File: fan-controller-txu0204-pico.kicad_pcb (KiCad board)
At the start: 2 copper layers, 21 x 67.7 mm, 58 parts, among them CN1 PWR, CN2 RaspberryPi_Pico, CN3 RaspberryPi_Pico, Q1 RU1C002ZP, U1 TPS259472A, U2 TXU0204, U3 TXU0204

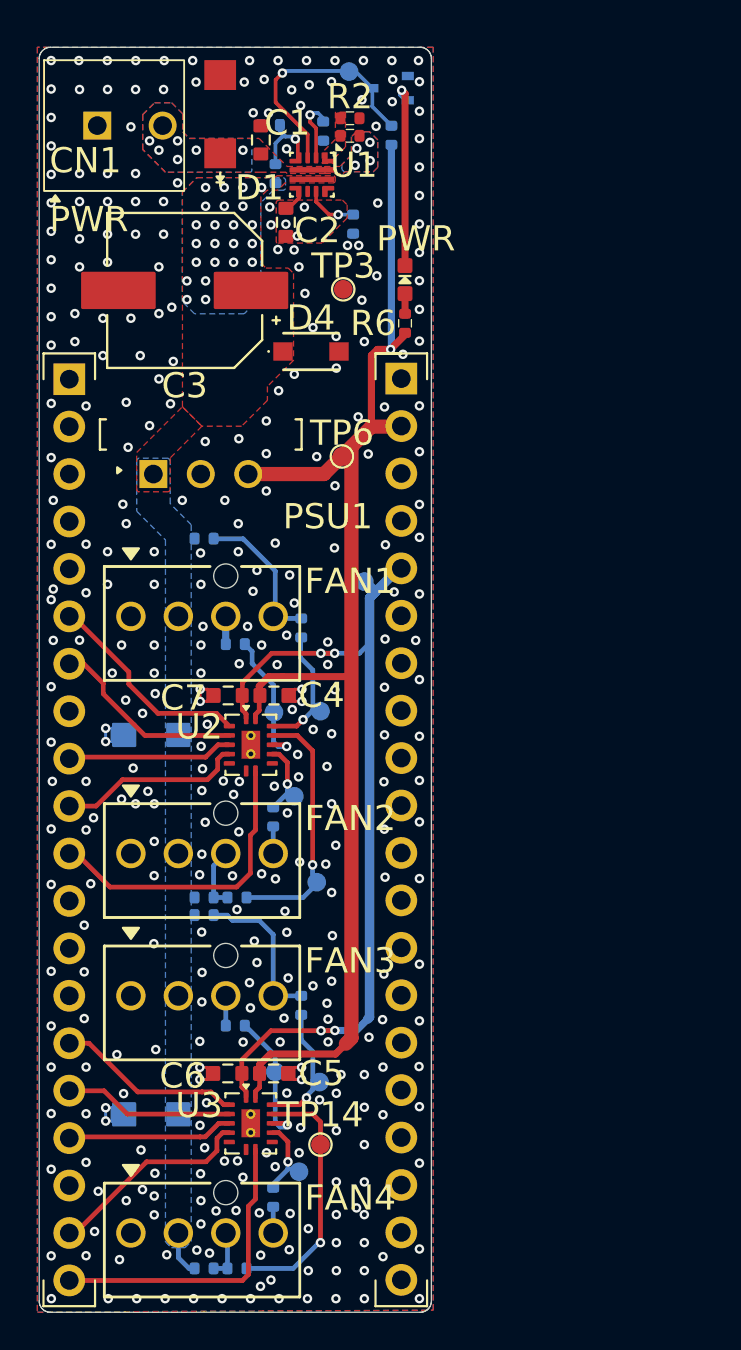
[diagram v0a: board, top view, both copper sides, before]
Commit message: tl;dr: switched to 4-layer pcb, overhauled 12vdc rail and protections, added 5vdc ORing ======================================================================== added:   ./       .gitignore - ignore lockfile
------------------------------------------------------------------------
removed:
  licenses/ - switched fonts to all WebPlus_ToshibaSat_8x14 and 9x16
      curie-LICENSE.txt
      curie-NOTICE.txt
      scientifica-LICENSE.txt
      scientifica-NOTICE.txt

------------------------------------------------------------------------
modified:
  ./
      README.md - updated to reflect changes in design
      fan-controller-pico_hmi.kicad_sch - added connector circuit, added
        pico pin connections
      fan-controller-txu0204-pico.kicad_pcb - changed to 4-layer design,
        changed protection circuit designs to use p-fet and polyfuse,
        split 12vdc rail into separate lines for fans and dc-dc
        converter, added lm66200 ORing diode, changed various netclass
        clearances, adjusted positions of tvs diodes for the fans'
        +12vdc pins
      fan-controller-txu0204-pico.kicad_sch - removed efuse, switched to
        p-fet reverse polarity protection, polyfuse for dc-dc converter,
        changed tvs diode for power connector to something more robust,
        added lm66200 ORing dual ideal diode for dc-dc converter 5v
        output and vbus to vsys control
      fan-controller-txu0204-pico.kicad_pro - see above
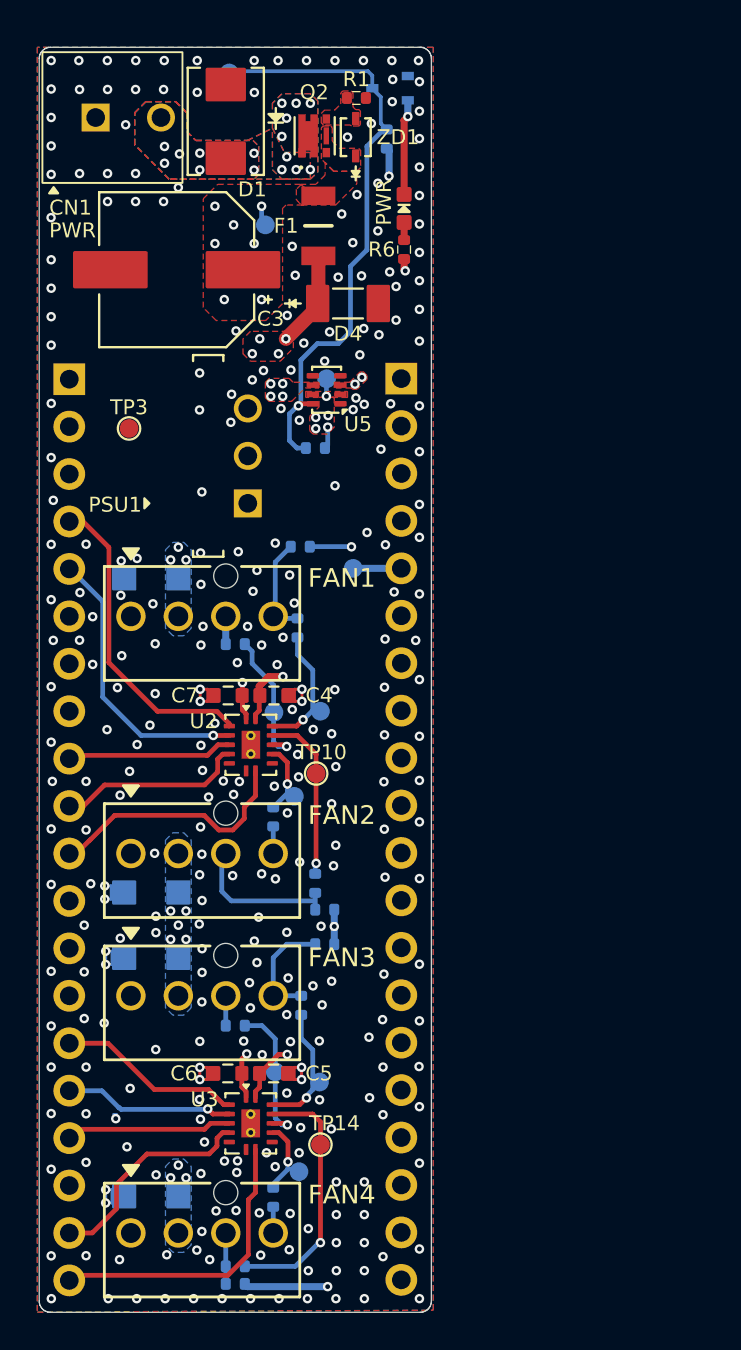
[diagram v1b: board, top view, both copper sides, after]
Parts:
- removed C1: 10uF, lsc-capacitors-added:C_GRM18_0603_1608Metric_MURATA
- removed C2: 0.56nF, lsc-capacitors-added:C_GRM18_0603_1608Metric_MURATA
- removed R2: 97.6k, lsc-resistor:R_RK37H_0402_1005Metric_KOA
- removed R3: 390k, lsc-resistor:R_RK37H_0402_1005Metric_KOA
- removed R4: 2.43k, lsc-resistor:R_RK37H_0402_1005Metric_KOA
- removed R5: 47k, lsc-resistor:R_RK37H_0402_1005Metric_KOA
- removed R7: 5.5k, lsc-resistor:R_RK37H_0402_1005Metric_KOA
- removed U1: TPS259472A, lsc-qfn:VFQFN10_RPW0010A_TI
- added D5: SMF12A, lsc-diode-smd:D_SOD-123F_EATON, B.Cu at (66.1, 92.2)
- added D6: SMF12A, lsc-diode-smd:D_SOD-123F_EATON, B.Cu at (66.1, 88.8)
- added F1: 2016L150/33DR, lsc-polyfuse:PTS1206_FUSC3216X68N_EATON, F.Cu at (75.0, 53.0)
- added Q2: DMP3014SFDE, lsc-dfn-vdfn-tdfn:TRANS_6-UDFN_U-DFN2020-6-E_DIO, F.Cu at (74.8, 48.2)
- added R9: 5.62k, lsc-resistor:R_RK37H_0402_1005Metric_KOA, B.Cu at (74.9, 65.0)
- added U5: LM66200, lsc-standard-chip-carrier:SOT-583_SOT-5X3_DRL0008A_TEX, F.Cu at (75.5, 61.8)
- added ZD1: MM3Z20B-AQ, lsc-diode-smd:D_SOD-323F_SOD323F_DIODES, F.Cu at (77.0, 48.3)
- CN2, CN3, TP6: moved to B.Cu
- D1: value TPSMA6L12A -> SMAJ16CA; footprint lsc-diode-smd:DIO_DO221AC_TPSMA6LSeries_LTF -> lsc-diode-smd:DIO_SMB_LOWVOLTAGE_DIODES
- D4: value RBS1MM40A -> SGL1-20; footprint lsc-diode-smd:CR_RBS1MM_ROM -> lsc-diode-smd:DIO_DO213AA_MINIMELF
- R1: value 470k -> 274
- R11, R12, R15, R16, R17, R18, R23, R24: value 10k -> 750
- R21, R22, R25, R26: value 7.5k -> 750
- TP10: moved to F.Cu
- moved TP3 13.7 mm to (64.9, 63.9)
- moved D2 8.38 mm to (66.1, 71.9)
- moved R22 6.65 mm to (75.4, 91.5), turned to 0 degrees
- moved R25 6.49 mm to (75.4, 89.7), turned to 0 degrees
- moved TP8 6.42 mm to (70.3, 44.9)
- moved TP10 5.82 mm to (74.9, 82.4)
- moved R21 5.17 mm to (74.1, 70.2), turned to 0 degrees
- moved D3 4.39 mm to (66.1, 105.0)
- moved R23 4.26 mm to (74.9, 88.3), turned to 90 degrees
- moved TP6 4.24 mm to (75.5, 61.2)
- moved R6 3.95 mm to (79.6, 54.3)
- moved LD1 3.81 mm to (79.6, 52.1)
- moved TP2 3.67 mm to (72.2, 53.0)
- moved D4 3.24 mm to (76.6, 57.2)
- moved PSU1 2.44 mm to (71.1, 65.4), turned to 90 degrees
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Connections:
- net /3V3 renamed +3.3VDC
- net /PWRGD renamed /LM66200_STAT
- C3 pad 1: /+12V_PROTECTED -> +12VDC
- C4 pad 1: /VSYS -> +5VDC
- C5 pad 1: /VSYS -> +5VDC
- CN2 pad 4: /GPIO2 -> /PICO_PWM_FAN1
- CN2 pad 5: /GPIO3 -> /PICO_PWM_FAN2
- CN2 pad 6: /PICO_PWM_FAN1 -> /Fan Controller Pico: HMI/I2C_SDA
- CN2 pad 7: /PICO_PWM_FAN2 -> /Fan Controller Pico: HMI/I2C_SCL
- CN3 pad 39: /VSYS -> +5VDC
- CN3 pad 40: /VBUS -> VBUS
- D2 pad 1: /+12V_PROTECTED -> +12VDC
- D3 pad 1: /+12V_PROTECTED -> +12VDC
- D4 pad 1: /+12V_PROTECTED -> /+12V_FUSED_PSU1
- FAN1 pad 2: /+12V_PROTECTED -> +12VDC
- FAN2 pad 2: /+12V_PROTECTED -> +12VDC
- FAN3 pad 2: /+12V_PROTECTED -> +12VDC
- FAN4 pad 2: /+12V_PROTECTED -> +12VDC
- PSU1 pad 1: /+12V_PROTECTED -> /+12V_FUSED_PSU1
- PSU1 pad 3: /VSYS -> /5V_PSU1_OUT
- R1 pad 1: /EN/UVLO -> GND
- R1 pad 2: /+12V_UNPROTECTED -> /V_{GS}_LIM
- R21 pad 2: /+12V_PROTECTED -> +5VDC
- R22 pad 2: /+12V_PROTECTED -> +5VDC
- R25 pad 2: /+12V_PROTECTED -> +5VDC
- R26 pad 2: /+12V_PROTECTED -> +5VDC
- R6 pad 2: /VSYS -> +5VDC
- R8 pad 2: /VSYS -> +5VDC
- TP2 pad 1: /+12V_PROTECTED -> +12VDC
- TP6 pad 1: /VSYS -> +5VDC
- U2 pad 14: /VSYS -> +5VDC
- U3 pad 14: /VSYS -> +5VDC
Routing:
- net +5VDC: track 0.00 -> 89.8 mm, vias 0 -> 12
- net /VSYS: track 72.5 -> 0.00 mm, vias 1 -> 0
- net /LM66200_STAT: track 13.1 -> 32.0 mm
- net /+12V_FUSED_PSU1: track 0.00 -> 15.5 mm, vias 0 -> 4
- net /PICO_PWM_FAN1: track 11.2 -> 16.8 mm
- net Net-(LD1-K): track 10.1 -> 5.29 mm
- net Net-(FAN2-Pin_3): track 3.37 -> 8.19 mm
- net /PICO_PWM_FAN2: track 10.5 -> 15.3 mm, vias 0 -> 1
- net /PWM_FAN2: track 13.6 -> 9.18 mm
- net /PGTH: track 4.35 -> 0.00 mm, vias 1 -> 0
- net /OVCSEL: track 3.48 -> 0.00 mm, vias 1 -> 0
- net /ILIM: track 2.82 -> 0.00 mm, vias 1 -> 0
- net /ENABLE_FAN1FAN2: track 16.3 -> 13.6 mm
- net Net-(FAN1-Pin_4): track 8.10 -> 5.53 mm
- net /+12V_PROTECTED: track 2.43 -> 0.00 mm, vias 23 -> 0
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- added copper zone on B.Cu, net +12VDC
- added copper zone on F.Cu, net +12VDC
- added copper zone on In2.Cu, net +12VDC
- added copper zone on F.Cu, net +5VDC
- added copper zone on In1.Cu, net +5VDC
- added copper zone on F.Cu, net /+12V_FUSED_PSU1
- added copper zone on In2.Cu, net /+12V_FUSED_PSU1
- added copper zone on F.Cu, net /5V_PSU1_OUT
- added copper zone on In1.Cu, net /5V_PSU1_OUT
- added copper zone on F.Cu, net /V_{GS}_LIM
- added copper zone on In1.Cu, net GND
- added copper zone on In2.Cu, net GND
- added copper zone on F.Cu, net VBUS
- added copper zone on In2.Cu, net VBUS
- removed copper zone on B.Cu, net /+12V_PROTECTED
- removed copper zone on F.Cu, net /+12V_PROTECTED
- removed copper zone on F.Cu, net /EN/UVLO
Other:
- copper layers 2 -> 4
- rule pad_to_mask_clearance: 0 -> 0.0508

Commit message: tl;dr: update images, adjust rules, clean up notes, move 12v rail to power plane, adj signal traces
=======================================================================
added:
  misc/img/ - switch to 4-layer design from 2-layer
      2d-in1-cu.png
      2d-in2-cu.png

-----------------------------------------------------------------------
modified:
  ./ - adjusted rules, cleaned up signal trace routing
      fan-controller-txu0204-pico.kicad_dru
      fan-controller-txu0204-pico.kicad_pcb
      fan-controller-txu0204-pico.kicad_pro
      fan-controller-txu0204-pico.kicad_sch
  misc/img/ - update images
      2d-b-cu.png
      2d-f-cu.png
      schematic_fan1-fan2.png
      schematic_fan3-fan4.png
      schematic_overview.png
      schematic_pico-headers.png
      schematic_power-good-indicator.png
      schematic_power-supply-protection.png
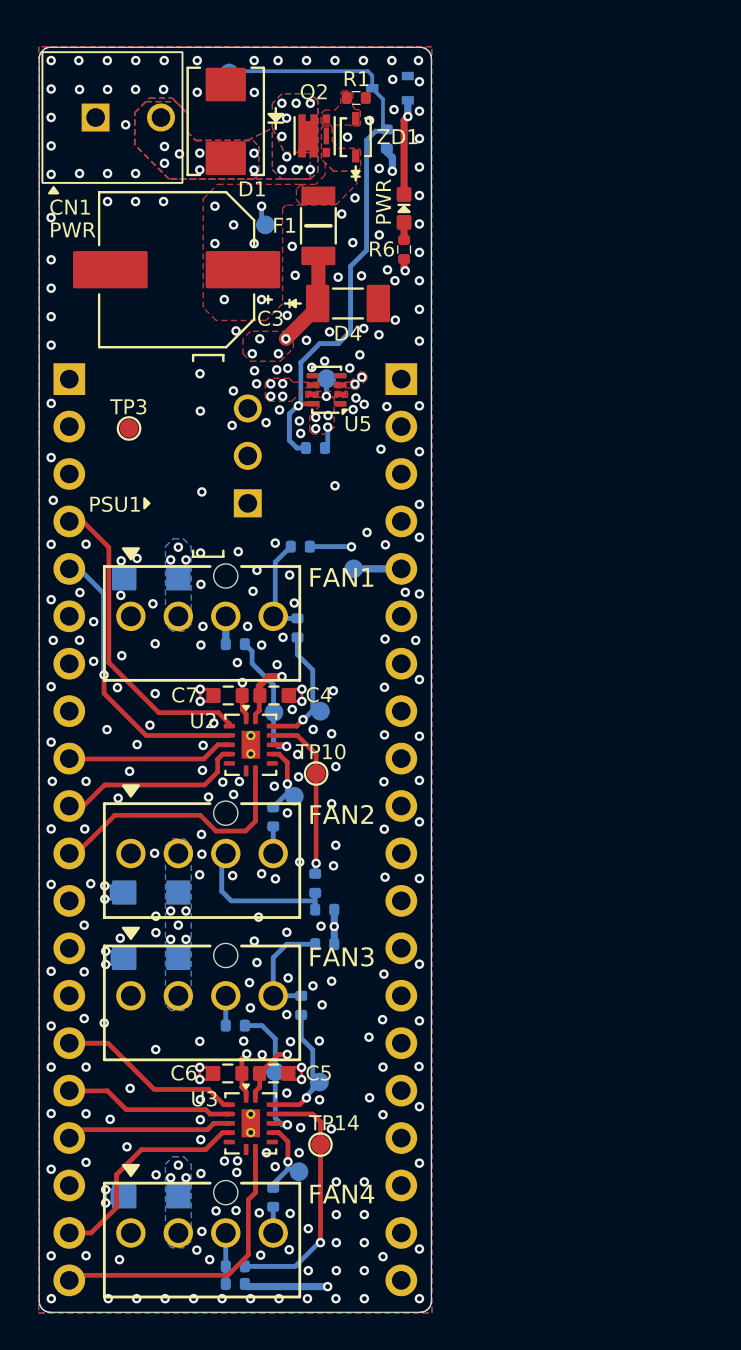
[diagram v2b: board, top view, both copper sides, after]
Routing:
- net +5VDC: track 89.8 -> 89.1 mm
- net /PICO_PWM_FAN4: track 9.10 -> 9.08 mm, vias 1 -> 0
- net GND: vias 298 -> 296
- added copper zone on In1.Cu, net +12VDC
- added copper zone on In1.Cu, net /+12V_FUSED_PSU1
- removed copper zone on In2.Cu, net +12VDC
- removed copper zone on In2.Cu, net /+12V_FUSED_PSU1

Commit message: tl;dr: re-added TVS protections to pwm and tach signals at fan connectors, rerouted 12v
========================================================================
added:
  misc/img/ - improved images for pcb etc
      fan-controller-txu0204-pico.svg
      fan-controller-txu0204-pico__Assembly.pdf
      fan-controller-txu0204-pico_color-b.svg
      fan-controller-txu0204-pico_color-f.svg
      fan-controller-txu0204-pico_color-in1.svg
      fan-controller-txu0204-pico_color-in2.svg

------------------------------------------------------------------------
removed:
  misc/img/ - restructured images of pcb
      2d-b-cu.png
      2d-b-cu_nocourtyards.png
      2d-f-cu.png
      2d-f-cu_nocourtyards.png
      2d-in1-cu.png
      2d-in2-cu.png

------------------------------------------------------------------------
modified:
  ./ - re-added TVS protections to tach and pwm signals at fan
    connectors, corrected some layout issues, rerouted 12vdc power to
    more effectively use the TVS diodes for the 12v power pins
      fan-controller-txu0204-pico.kicad_pcb
      fan-controller-txu0204-pico.kicad_pro
      fan-controller-txu0204-pico.kicad_sch

  misc/img/
      schematic_overview.png - re-added TVS protections to pwm and tach
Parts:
- added D10: DF3A5.6FV, lsc-transistor:TRANS_SOT-723, B.Cu at (71.3, 108.8)
- added D7: DF3A5.6FV, lsc-transistor:TRANS_SOT-723, B.Cu at (71.4, 75.9)
- added D8: DF3A5.6FV, lsc-transistor:TRANS_SOT-723, B.Cu at (71.4, 88.7)
- added D9: DF3A5.6FV, lsc-transistor:TRANS_SOT-723, B.Cu at (71.4, 96.2)
- TP10, TP14: moved to B.Cu
- TP16: moved to F.Cu
- moved TP14 9.72 mm to (69.1, 109.9)
- moved TP10 8.42 mm to (74.1, 90.8)
- moved R24 6.24 mm to (76.8, 109.0)
- moved TP8 5.30 mm to (75.5, 45.3)
- moved R26 5.04 mm to (75.5, 108.5), turned to 90 degrees
- moved R22 4.45 mm to (76.3, 95.9)
- moved R16 4.02 mm to (73.1, 88.7), turned to 0 degrees
- moved R17 3.97 mm to (75.1, 98.7)
- moved R15 3.90 mm to (75.1, 78.3)
- moved R21 3.86 mm to (75.1, 74.0)
- moved R11 3.82 mm to (72.5, 78.8), turned to -90 degrees
- moved R12 3.79 mm to (72.5, 99.2), turned to -90 degrees
- moved TP16 3.28 mm to (74.9, 106.8)
- moved TP11 3.28 mm to (69.8, 77.5)
- moved TP15 3.05 mm to (69.8, 97.5)
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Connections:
- FAN1 pad 3: Net-(FAN1-Pin_3) -> Net-(D7-K1)
- FAN1 pad 4: Net-(FAN1-Pin_4) -> Net-(D7-K2)
- FAN2 pad 3: Net-(FAN2-Pin_3) -> Net-(D8-K1)
- FAN2 pad 4: Net-(FAN2-Pin_4) -> Net-(D8-K2)
- FAN3 pad 3: Net-(FAN3-Pin_3) -> Net-(D9-K1)
- FAN3 pad 4: Net-(FAN3-Pin_4) -> Net-(D9-K2)
- FAN4 pad 3: Net-(FAN4-Pin_3) -> Net-(D10-K1)
- FAN4 pad 4: Net-(FAN4-Pin_4) -> Net-(D10-K2)
- R11 pad 1: Net-(FAN1-Pin_3) -> Net-(D7-K1)
- R12 pad 1: Net-(FAN3-Pin_3) -> Net-(D9-K1)
- R15 pad 1: Net-(FAN1-Pin_4) -> Net-(D7-K2)
- R16 pad 1: Net-(FAN2-Pin_4) -> Net-(D8-K2)
- R17 pad 1: Net-(FAN3-Pin_4) -> Net-(D9-K2)
- R18 pad 1: Net-(FAN4-Pin_4) -> Net-(D10-K2)
- R21 pad 1: Net-(FAN1-Pin_4) -> Net-(D7-K2)
- R22 pad 1: Net-(FAN3-Pin_4) -> Net-(D9-K2)
- R23 pad 1: Net-(FAN2-Pin_3) -> Net-(D8-K1)
- R24 pad 1: Net-(FAN4-Pin_3) -> Net-(D10-K1)
- R25 pad 1: Net-(FAN2-Pin_3) -> Net-(D8-K1)
- R26 pad 1: Net-(FAN4-Pin_3) -> Net-(D10-K1)
- TP10 pad 1: /PWM_FAN2 -> Net-(D8-K1)
- TP11 pad 1: /TACH_FAN1 -> Net-(D7-K1)
- TP12 pad 1: /TACH_FAN2 -> Net-(D8-K2)
- TP13 pad 1: /PWM_FAN3 -> Net-(D9-K2)
- TP14 pad 1: /PWM_FAN4 -> Net-(D10-K1)
- TP15 pad 1: /TACH_FAN3 -> Net-(D9-K1)
- TP16 pad 1: /TACH_FAN4 -> Net-(D10-K2)
- TP9 pad 1: /PWM_FAN1 -> Net-(D7-K2)
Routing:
- net +12VDC: track 1.08 -> 66.8 mm
- net Net-(D10-K1): track 0.00 -> 10.9 mm
- net Net-(D8-K1): track 0.00 -> 10.3 mm
- net Net-(D7-K2): track 0.00 -> 9.01 mm
- net +5VDC: track 89.1 -> 80.8 mm, vias 12 -> 16
- net Net-(FAN2-Pin_3): track 8.19 -> 0.00 mm
- net Net-(D9-K2): track 0.00 -> 8.15 mm
- net Net-(D7-K1): track 0.00 -> 7.65 mm
- net Net-(D9-K1): track 0.00 -> 7.64 mm
- net Net-(D10-K2): track 0.00 -> 6.31 mm, vias 0 -> 1
- net Net-(FAN3-Pin_4): track 5.99 -> 0.00 mm
- net /LM66200_STAT: track 32.2 -> 26.4 mm, vias 1 -> 5
- net Net-(FAN1-Pin_4): track 5.53 -> 0.00 mm
- net Net-(D8-K2): track 0.00 -> 4.95 mm
- net /TACH_FAN2: track 3.71 -> 8.19 mm
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- added copper zone on In2.Cu, net +3.3VDC
- added copper zone on In2.Cu, net +5VDC
- added copper zone on In1.Cu, net /+12V_UNPROTECTED
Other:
- board text added: "12V"
- board text added: "B - SIG"
- board text added: "F - SIG"
- board text added: "GND"
- board text added: "IN1 - PWR"
- board text added: "IN2 - GND"
